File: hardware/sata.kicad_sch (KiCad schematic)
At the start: 0 parts

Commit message: Switch from JMS578 USB-to-SATA to ASM1061 PCIe-to-SATA
No proprietary firmware blob required. Native AHCI driver in Linux.
SMART works directly without SAT translation.
4-layer PCB with 100Ω differential impedance for PCIe Gen 2.
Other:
- title: Offsite Backup Device - SATA Bridge -> Offsite Backup Device - ASM1061 PCIe-to-SATA
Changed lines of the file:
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@@
 	(paper "A4")
 	(title_block
-		(title "Offsite Backup Device - SATA Bridge")
+		(title "Offsite Backup Device - ASM1061 PCIe-to-SATA")
 		(date "2026-04-07")
 		(rev "0.1")

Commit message: Rename project to Granit
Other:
- company: https://github.com/laenzlinger/offsite-backup -> https://github.com/laenzlinger/granit
- title: Offsite Backup Device - ASM1061 PCIe-to-SATA -> Granit — ASM1061 PCIe-to-SATA
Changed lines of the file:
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@@
 	(paper "A4")
 	(title_block
-		(title "Offsite Backup Device - ASM1061 PCIe-to-SATA")
+		(title "Granit — ASM1061 PCIe-to-SATA")
 		(date "2026-04-07")
 		(rev "0.1")
-		(company "https://github.com/laenzlinger/offsite-backup")
+		(company "https://github.com/laenzlinger/granit")
 		(comment 1 "License: CERN Open Hardware Licence Version 2 - Permissive")
 		(comment 2 "Git commit hash: ${GIT_HASH}")

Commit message: SATA: place ASM1061, connect GND and power pins
- ASM1061 symbol + footprint from Component Search Engine
- All GND pins connected (including EP and VSSPWM)
- 3.3V pins connected with 100nF decoupling caps
- 1.2V internal regulator pins tied together
- 29 ASM1061 pins remaining (PCIe, SATA, crystal, misc)
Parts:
- added C42, C43, C44, C45, C46: 100n, Capacitor_SMD:C_0805_2012Metric, symbol Device:C_Small
- added IC1: ASM1061, QFN50P700X700X90-49N-D, symbol granit:ASM1061
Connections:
- new net: IC1.11 (VCC12_2), IC1.12 (VDD12S_1), IC1.25 (VDD12S_2), IC1.30 (VDD12P), IC1.43 (VCC12_3), IC1.48 (VCC12_4), IC1.7 (VCC12_1)
- new net +3V3: C42.1, C43.1, C44.1, C45.1, C46.1, IC1.19 (VCC33S), IC1.3 (VCC33IN), IC1.36 (VCC33P), IC1.44 (VCC33_2), IC1.9 (VCC33_1)
- new net GND: C42.2, C43.2, C44.2, C45.2, C46.2, IC1.1 (VSSPWM), IC1.10 (GND_2), IC1.15 (GNDA_1), IC1.22 (GNDA_2), IC1.33 (GNDA_3), IC1.42 (GND_3), IC1.49 (EP), IC1.8 (GND_1)

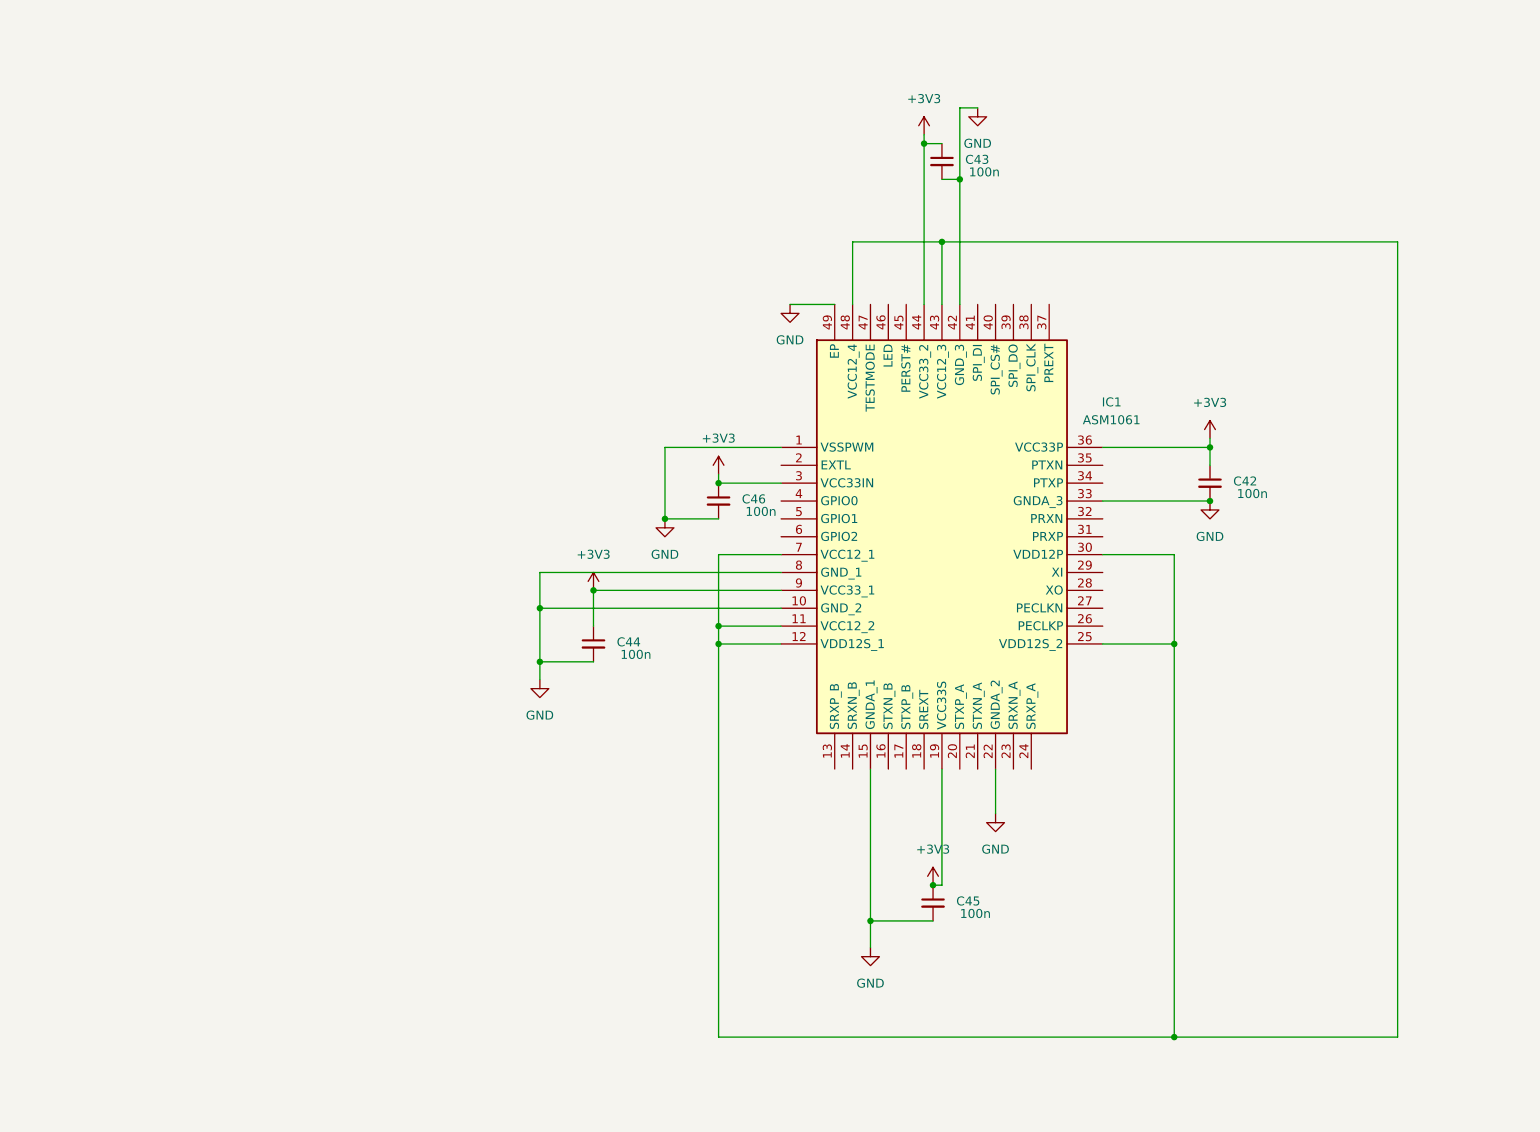
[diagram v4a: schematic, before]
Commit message: SATA: ASM1061 fully wired
- PCIe data, clock, and reset connected via global labels
- 25MHz crystal with load caps
- SATA Port A connected to 7-pin data connector
- SATA Port B NC'd
- Impedance calibration resistors (SREXT 750Ω, PREXT 750Ω, EXTL 12kΩ)
- SPI flash pins NC'd (no firmware needed)
- TESTMODE tied to GND
- All decoupling caps placed (5x 3.3V, 4x 1.2V)
- 6 ERC errors remaining (ETH_SYNC NC, PCIe_CLK_nREQ, USB_OTG_ID)
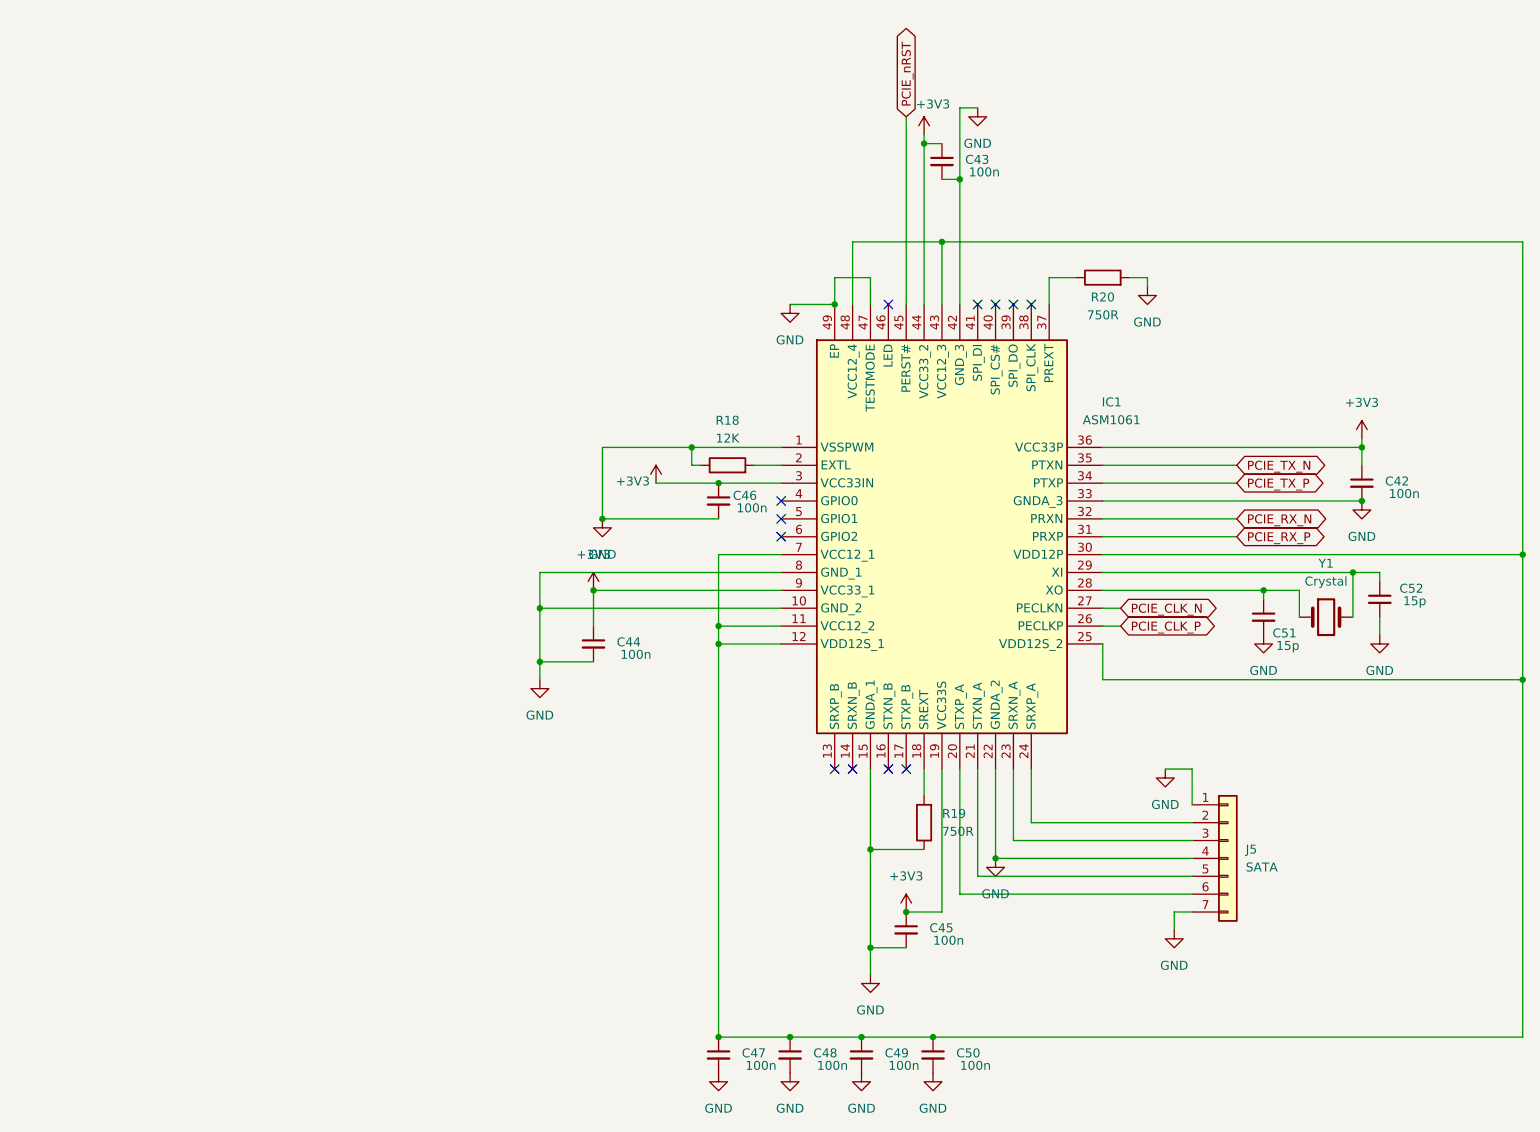
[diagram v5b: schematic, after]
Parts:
- added C47, C48, C49, C50: 100n, Capacitor_SMD:C_0805_2012Metric, symbol Device:C_Small
- added C51, C52: 15p, Capacitor_SMD:C_0805_2012Metric, symbol Device:C_Small
- added J5: SATA, symbol Connector_Generic:Conn_01x07
- added R18: 12K, symbol Device:R
- added R19, R20: 750R, symbol Device:R
- added Y1: Crystal, symbol Device:Crystal
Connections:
- net GND: now also IC1.47 (TESTMODE), C47.2, C48.2, C49.2, C50.2, C51.2, C52.2, J5.1 (Pin_1), J5.4 (Pin_4), J5.7 (Pin_7), R18.1, R19.1, R20.2
- net at IC1.11 (VCC12_2), IC1.12 (VDD12S_1), IC1.25 (VDD12S_2)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: now also C47.1, C48.1, C49.1, C50.1
- net at IC1.18 (SREXT): now also R19.2
- net at IC1.2 (EXTL): now also R18.2
- net at IC1.20 (STXP_A): now also J5.6 (Pin_6)
- net at IC1.21 (STXN_A): now also J5.5 (Pin_5)
- net at IC1.23 (SRXN_A): now also J5.3 (Pin_3)
- net at IC1.24 (SRXP_A): now also J5.2 (Pin_2)
- net PCIE_CLK_P: now reaches IC1.26 (PECLKP)
- net PCIE_CLK_N: now reaches IC1.27 (PECLKN)
- net at IC1.28 (XO): now also C51.1, Y1.1
- net at IC1.29 (XI): now also C52.1, Y1.2
- net PCIE_RX_P: now reaches IC1.31 (PRXP)
- net PCIE_RX_N: now reaches IC1.32 (PRXN)
- net PCIE_TX_P: now reaches IC1.34 (PTXP)
- net PCIE_TX_N: now reaches IC1.35 (PTXN)
- net at IC1.37 (PREXT): now also R20.1
- net PCIE_nRST: now reaches IC1.45 (PERST#)
- no-connect marks 0 -> 12
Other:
- moved on the sheet: C42, C45

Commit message: ERC: 0 errors, 0 warnings — fully clean
- Fix ASM1061 footprint reference (granit:QFN50P700X700X90-49N-D)
- Fix CM4 embedded symbol references (pedalboard → granit)
- Sync ASM1061 embedded symbol with library
- Remove dangling no-connect flags
- Re-add NC for barrel jack switch pin (J7 pin 3)
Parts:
- IC1: footprint QFN50P700X700X90-49N-D -> granit:QFN50P700X700X90-49N-D
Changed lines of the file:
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@@
 			)
 		)
-		(property "Footprint" "QFN50P700X700X90-49N-D"
+		(property "Footprint" "granit:QFN50P700X700X90-49N-D"
 			(at 163.83 158.42 0)
 			(hide yes)

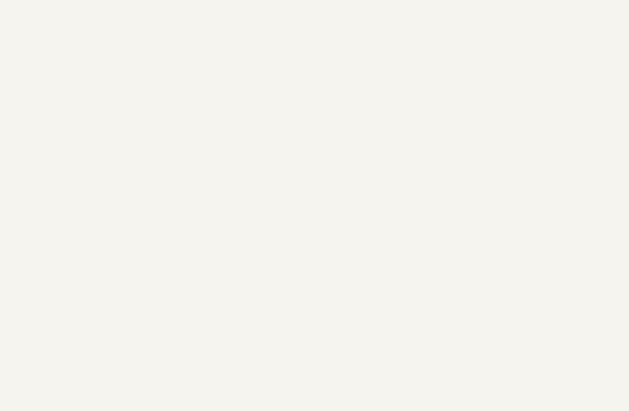
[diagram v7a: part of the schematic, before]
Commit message: SATA: add power connector (12V, 5V, 3.3V, GND)
- 12V passthrough from PSU (after polarity protection)
- 5V from AP64501SP-13 buck
- 3.3V from NCP1117 LDO (for completeness)
- FIXME: TPM/crypto chip added to TODO
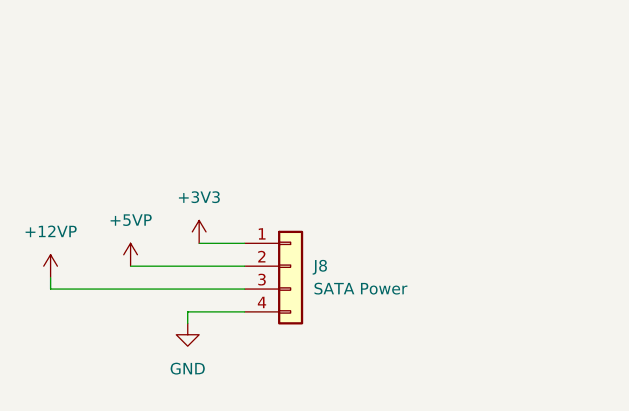
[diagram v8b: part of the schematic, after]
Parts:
- added J8: SATA Power, symbol Connector_Generic:Conn_01x04
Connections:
- net +3V3: now also J8.1 (Pin_1)
- net GND: now also J8.4 (Pin_4)
- new net +12VP: J8.3 (Pin_3)
- new net +5VP: J8.2 (Pin_2)
